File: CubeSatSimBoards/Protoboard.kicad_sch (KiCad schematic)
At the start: 5 parts, among them J1 Conn_02x20_Odd_Even

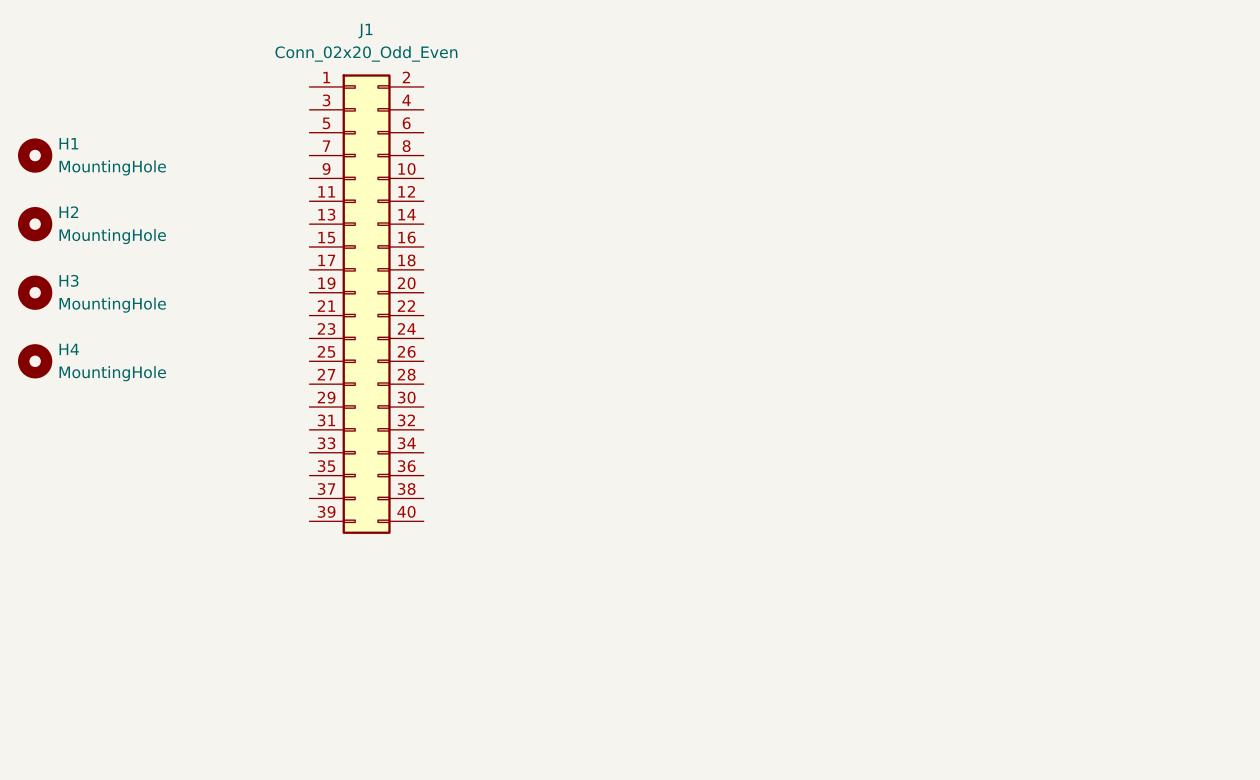
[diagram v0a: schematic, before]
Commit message: Added cutouts, brokenout Pi header pins and label to protoboard
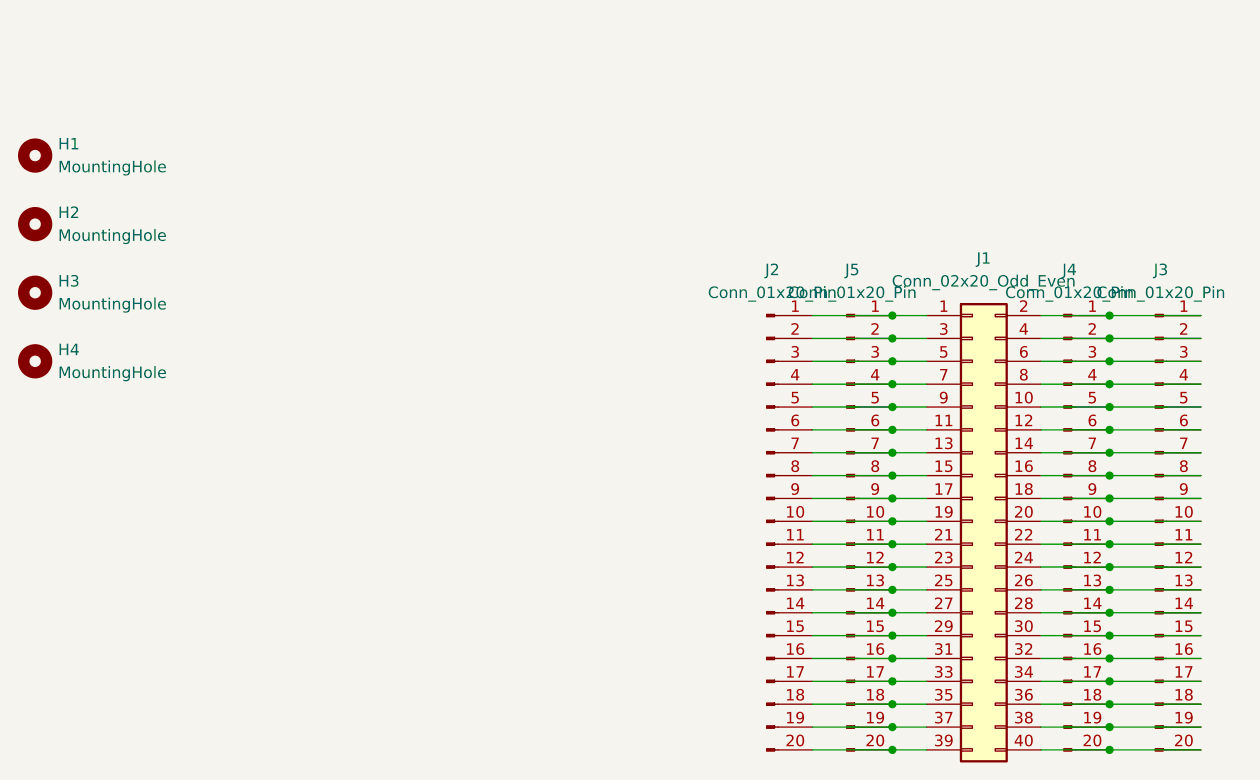
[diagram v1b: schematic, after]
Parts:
- added J2, J3, J4, J5: Conn_01x20_Pin, Connector_PinHeader_2.54mm:PinHeader_1x20_P2.54mm_Vertical, symbol Connector:Conn_01x20_Pin
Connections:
- net at J1.1 (Pin_1): now also J2.1 (Pin_1), J5.1 (Pin_1)
- net at J1.10 (Pin_10): now also J3.5 (Pin_5), J4.5 (Pin_5)
- net at J1.11 (Pin_11): now also J2.6 (Pin_6), J5.6 (Pin_6)
- net at J1.12 (Pin_12): now also J3.6 (Pin_6), J4.6 (Pin_6)
- net at J1.13 (Pin_13): now also J2.7 (Pin_7), J5.7 (Pin_7)
- net at J1.14 (Pin_14): now also J3.7 (Pin_7), J4.7 (Pin_7)
- net at J1.15 (Pin_15): now also J2.8 (Pin_8), J5.8 (Pin_8)
- net at J1.16 (Pin_16): now also J3.8 (Pin_8), J4.8 (Pin_8)
- net at J1.17 (Pin_17): now also J2.9 (Pin_9), J5.9 (Pin_9)
- net at J1.18 (Pin_18): now also J3.9 (Pin_9), J4.9 (Pin_9)
- net at J1.19 (Pin_19): now also J2.10 (Pin_10), J5.10 (Pin_10)
- net at J1.2 (Pin_2): now also J3.1 (Pin_1), J4.1 (Pin_1)
- net at J1.20 (Pin_20): now also J3.10 (Pin_10), J4.10 (Pin_10)
- net at J1.21 (Pin_21): now also J2.11 (Pin_11), J5.11 (Pin_11)
- net at J1.22 (Pin_22): now also J3.11 (Pin_11), J4.11 (Pin_11)
- net at J1.23 (Pin_23): now also J2.12 (Pin_12), J5.12 (Pin_12)
- net at J1.24 (Pin_24): now also J3.12 (Pin_12), J4.12 (Pin_12)
- net at J1.25 (Pin_25): now also J2.13 (Pin_13), J5.13 (Pin_13)
- net at J1.26 (Pin_26): now also J3.13 (Pin_13), J4.13 (Pin_13)
- net at J1.27 (Pin_27): now also J2.14 (Pin_14), J5.14 (Pin_14)
- net at J1.28 (Pin_28): now also J3.14 (Pin_14), J4.14 (Pin_14)
- net at J1.29 (Pin_29): now also J2.15 (Pin_15), J5.15 (Pin_15)
- net at J1.3 (Pin_3): now also J2.2 (Pin_2), J5.2 (Pin_2)
- net at J1.30 (Pin_30): now also J3.15 (Pin_15), J4.15 (Pin_15)
- net at J1.31 (Pin_31): now also J2.16 (Pin_16), J5.16 (Pin_16)
- net at J1.32 (Pin_32): now also J3.16 (Pin_16), J4.16 (Pin_16)
- net at J1.33 (Pin_33): now also J2.17 (Pin_17), J5.17 (Pin_17)
- net at J1.34 (Pin_34): now also J3.17 (Pin_17), J4.17 (Pin_17)
- net at J1.35 (Pin_35): now also J2.18 (Pin_18), J5.18 (Pin_18)
- net at J1.36 (Pin_36): now also J3.18 (Pin_18), J4.18 (Pin_18)
- net at J1.37 (Pin_37): now also J2.19 (Pin_19), J5.19 (Pin_19)
- net at J1.38 (Pin_38): now also J3.19 (Pin_19), J4.19 (Pin_19)
- net at J1.39 (Pin_39): now also J2.20 (Pin_20), J5.20 (Pin_20)
- net at J1.4 (Pin_4): now also J3.2 (Pin_2), J4.2 (Pin_2)
- net at J1.40 (Pin_40): now also J3.20 (Pin_20), J4.20 (Pin_20)
- net at J1.5 (Pin_5): now also J2.3 (Pin_3), J5.3 (Pin_3)
- net at J1.6 (Pin_6): now also J3.3 (Pin_3), J4.3 (Pin_3)
- net at J1.7 (Pin_7): now also J2.4 (Pin_4), J5.4 (Pin_4)
- net at J1.8 (Pin_8): now also J3.4 (Pin_4), J4.4 (Pin_4)
- net at J1.9 (Pin_9): now also J2.5 (Pin_5), J5.5 (Pin_5)
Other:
- moved on the sheet: J1
